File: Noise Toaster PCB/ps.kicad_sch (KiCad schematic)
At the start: 9 parts

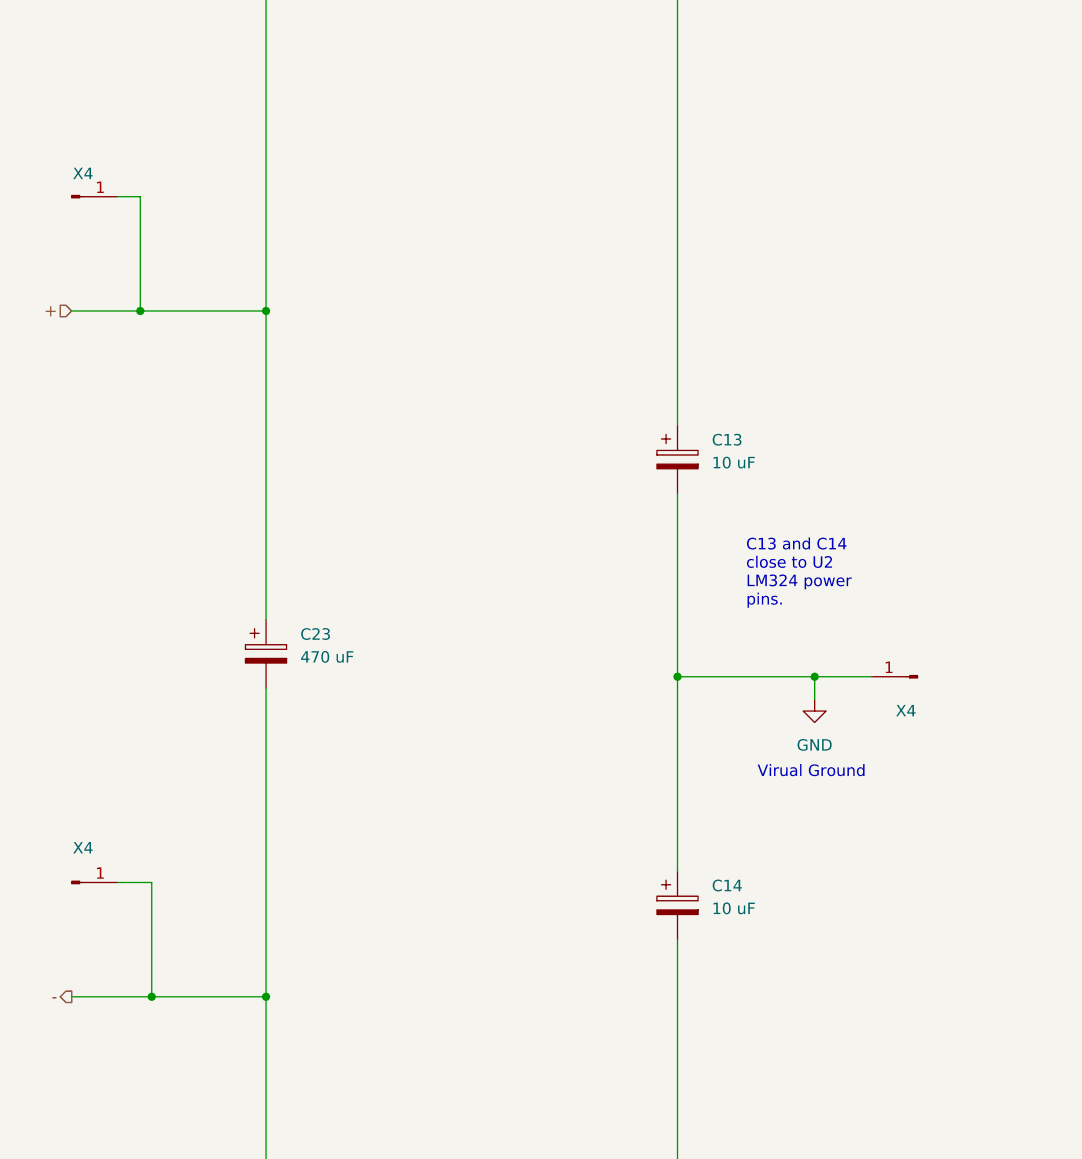
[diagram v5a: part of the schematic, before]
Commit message: changed header pins to groups
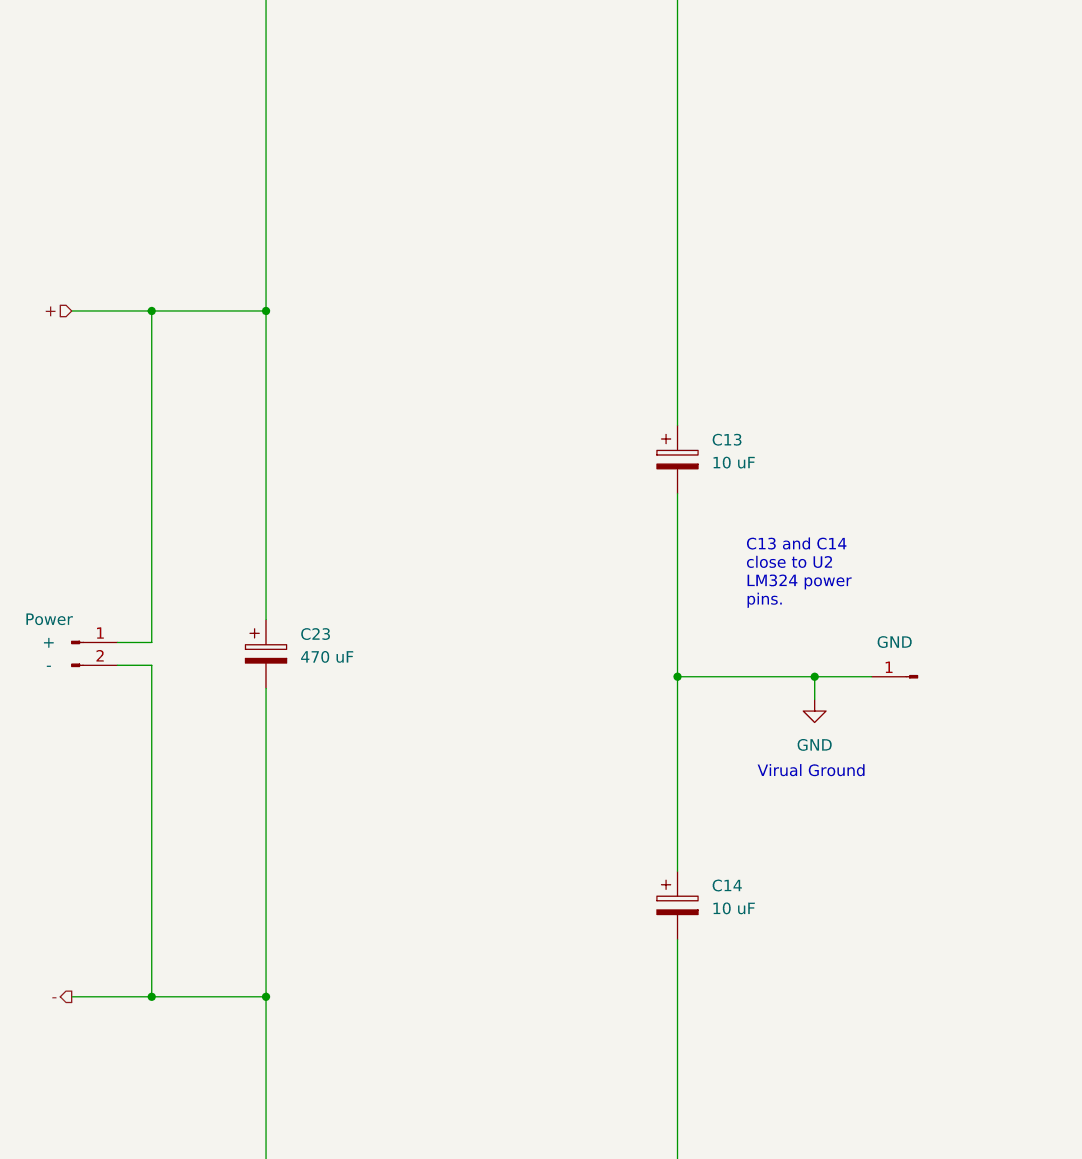
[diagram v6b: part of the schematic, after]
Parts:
- removed X4 (x2): ~, Connector_PinHeader_1.00mm:PinHeader_1x01_P1.00mm_Vertical, symbol Connector:Conn_01x01_Pin
- added J2: Power, Connector_PinHeader_2.00mm:PinHeader_1x02_P2.00mm_Vertical, symbol Connector:Conn_01x02_Pin
- X4: value ~ -> GND; footprint Connector_PinHeader_1.00mm:PinHeader_1x01_P1.00mm_Vertical -> Connector_PinHeader_2.00mm:PinHeader_1x01_P2.00mm_Vertical
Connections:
- net B+: now also J2.1 (Pin_1)
- net B-: now also J2.2 (Pin_2)
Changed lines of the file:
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@@
   (title_block
     (title "Power Supply")
-    (rev "0.5")
+    (rev "0.6")
     (company "Music From Outer Space LLC")
     (comment 1 "Licence: CC-BY-NC-SA")
@@
   (junction (at 59.69 139.7) (diameter 0) (color 0 0 0 0)
   )
-  (junction (at 45.72 63.5) (diameter 0) (color 0 0 0 0)
+  (junction (at 46.99 63.5) (diameter 0) (color 0 0 0 0)
   )
   (junction (at 46.99 139.7) (diameter 0) (color 0 0 0 0)
@@
     (stroke (width 0) (type default))
   )
-  (wire (pts (xy 46.99 127) (xy 46.99 139.7))
+  (wire (pts (xy 46.99 102.87) (xy 46.99 139.7))
     (stroke (width 0) (type default))
   )
@@
     (stroke (width 0) (type default))
   )
-  (wire (pts (xy 43.18 127) (xy 46.99 127))
-    (stroke (width 0) (type default))
-  )
   (wire (pts (xy 160.02 105.41) (xy 160.02 133.35))
     (stroke (width 0) (type default))
   )
-  (wire (pts (xy 38.1 63.5) (xy 45.72 63.5))
+  (wire (pts (xy 46.99 102.87) (xy 43.18 102.87))
     (stroke (width 0) (type default))
   )
@@
     (stroke (width 0) (type default))
   )
+  (wire (pts (xy 43.18 100.33) (xy 46.99 100.33))
+    (stroke (width 0) (type default))
+  )
   (wire (pts (xy 105.41 83.82) (xy 105.41 104.14))
     (stroke (width 0) (type default))
@@
     (stroke (width 0) (type default))
   )
-  (wire (pts (xy 45.72 50.8) (xy 45.72 63.5))
+  (wire (pts (xy 46.99 63.5) (xy 46.99 100.33))
     (stroke (width 0) (type default))
   )
@@
     (stroke (width 0) (type default))
   )
-  (wire (pts (xy 43.18 50.8) (xy 45.72 50.8))
-    (stroke (width 0) (type default))
-  )
   (wire (pts (xy 59.69 139.7) (xy 59.69 176.53))
     (stroke (width 0) (type default))
@@
     (stroke (width 0) (type default))
   )
-  (wire (pts (xy 45.72 63.5) (xy 59.69 63.5))
-    (stroke (width 0) (type default))
-  )
   (wire (pts (xy 120.65 106.68) (xy 120.65 104.14))
     (stroke (width 0) (type default))
@@
     (stroke (width 0) (type default))
   )
+  (wire (pts (xy 46.99 63.5) (xy 59.69 63.5))
+    (stroke (width 0) (type default))
+  )
   (wire (pts (xy 224.79 105.41) (xy 224.79 116.84))
+    (stroke (width 0) (type default))
+  )
+  (wire (pts (xy 38.1 63.5) (xy 46.99 63.5))
     (stroke (width 0) (type default))
   )
@@
     (effects (font (size 1.27 1.27)) (justify right))
   )
-  (symbol (lib_id "Connector:Conn_01x01_Pin") (at 38.1 127 0) (unit 1)
-    (in_bom yes) (on_board yes) (dnp no)
-    (property "Reference" "X4" (at 39.37 123.19 0)
-      (effects (font (size 1.27 1.27)))
-    )
-    (property "Value" "~" (at 38.735 124.46 0)
-      (effects (font (size 1.27 1.27)))
-    )
-    (property "Footprint" "Connector_PinHeader_1.00mm:PinHeader_1x01_P1.00mm_Vertical" (at 38.1 127 0)
-      (effects (font (size 1.27 1.27)) hide)
-    )
-    (property "Datasheet" "~" (at 38.1 127 0)
-      (effects (font (size 1.27 1.27)) hide)
-    )
-    (pin "1")
-    (instances
-      (project "Noise Toaster PCB"
-        (path "/7be3f398-d902-4566-9ee4-0bff072cd47e/818b46cb-815d-4132-b52d-9731333b7f1f"
-          (reference "X4") (unit 1)
-        )
-        (path "/7be3f398-d902-4566-9ee4-0bff072cd47e/d0369b76-3398-4137-86ba-22490a5aca99"
-          (reference "X22") (unit 1)
-        )
-        (path "/7be3f398-d902-4566-9ee4-0bff072cd47e/0647ade8-e724-4924-aa52-6cbb42374298"
-          (reference "X22") (unit 1)
-        )
-        (path "/7be3f398-d902-4566-9ee4-0bff072cd47e/8163954c-0389-42ef-b929-449d078595e3"
-          (reference "X-1") (unit 1)
-        )
-      )
-    )
-  )
-  (symbol (lib_id "Connector:Conn_01x01_Pin") (at 38.1 50.8 0) (unit 1)
-    (in_bom yes) (on_board yes) (dnp no)
-    (property "Reference" "X4" (at 39.37 48.26 0)
-      (effects (font (size 1.27 1.27)))
-    )
-    (property "Value" "~" (at 38.735 48.26 0)
-      (effects (font (size 1.27 1.27)))
-    )
-    (property "Footprint" "Connector_PinHeader_1.00mm:PinHeader_1x01_P1.00mm_Vertical" (at 38.1 50.8 0)
-      (effects (font (size 1.27 1.27)) hide)
-    )
-    (property "Datasheet" "~" (at 38.1 50.8 0)
-      (effects (font (size 1.27 1.27)) hide)
-    )
-    (pin "1")
-    (instances
-      (project "Noise Toaster PCB"
-        (path "/7be3f398-d902-4566-9ee4-0bff072cd47e/818b46cb-815d-4132-b52d-9731333b7f1f"
-          (reference "X4") (unit 1)
-        )
-        (path "/7be3f398-d902-4566-9ee4-0bff072cd47e/d0369b76-3398-4137-86ba-22490a5aca99"
-          (reference "X22") (unit 1)
-        )
-        (path "/7be3f398-d902-4566-9ee4-0bff072cd47e/0647ade8-e724-4924-aa52-6cbb42374298"
-          (reference "X22") (unit 1)
-        )
-        (path "/7be3f398-d902-4566-9ee4-0bff072cd47e/8163954c-0389-42ef-b929-449d078595e3"
-          (reference "X+1") (unit 1)
-        )
-      )
-    )
-  )
   (symbol (lib_id "power:GND") (at 120.65 106.68 0) (unit 1)
     (in_bom yes) (on_board yes) (dnp no) (fields_autoplaced)
@@
     (in_bom yes) (on_board yes) (dnp no)
     (property "Reference" "X4" (at 130.81 107.95 0)
-      (effects (font (size 1.27 1.27)))
-    )
-    (property "Value" "~" (at 131.445 106.68 0)
-      (effects (font (size 1.27 1.27)))
-    )
-    (property "Footprint" "Connector_PinHeader_1.00mm:PinHeader_1x01_P1.00mm_Vertical" (at 132.08 104.14 0)
+      (effects (font (size 1.27 1.27)) hide)
+    )
+    (property "Value" "GND" (at 129.54 100.33 0)
+      (effects (font (size 1.27 1.27)))
+    )
+    (property "Footprint" "Connector_PinHeader_2.00mm:PinHeader_1x01_P2.00mm_Vertical" (at 132.08 104.14 0)
       (effects (font (size 1.27 1.27)) hide)
     )
@@
         )
       )
+    )
+  )
+  (symbol (lib_id "Connector:Conn_01x02_Pin") (at 38.1 100.33 0) (unit 1)
+    (in_bom yes) (on_board yes) (dnp no)
+    (property "Reference" "J2" (at 35.56 97.79 0)
+      (effects (font (size 1.27 1.27)) hide)
+    )
+    (property "Value" "Power" (at 35.56 97.79 0)
+      (effects (font (size 1.27 1.27)))
+    )
+    (property "Footprint" "Connector_PinHeader_2.00mm:PinHeader_1x02_P2.00mm_Vertical" (at 38.1 100.33 0)
+      (effects (font (size 1.27 1.27)) hide)
+    )
+    (property "Datasheet" "~" (at 38.1 100.33 0)
+      (effects (font (size 1.27 1.27)) hide)
+    )
+    (property "Positiv" "+" (at 35.56 100.33 0)
+      (effects (font (size 1.27 1.27)))
+    )
+    (property "Negativ" "-" (at 35.56 102.87 0)
+      (effects (font (size 1.27 1.27)))
+    )
+    (pin "1")
+    (pin "2")
+    (instances
+      (project "Noise Toaster PCB"
+        (path "/7be3f398-d902-4566-9ee4-0bff072cd47e/8163954c-0389-42ef-b929-449d078595e3"
+          (reference "J2") (unit 1)
+        )
+      )

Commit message: added front panel pcb
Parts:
- renumbered X4 to GND1
